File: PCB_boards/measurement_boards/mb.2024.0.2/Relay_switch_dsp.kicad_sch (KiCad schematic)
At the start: 8 parts, among them K1 G5LE-1, K2 G5LE-1, Q1 ZVN4206ASTZ, Q2 ZVN4206ASTZ

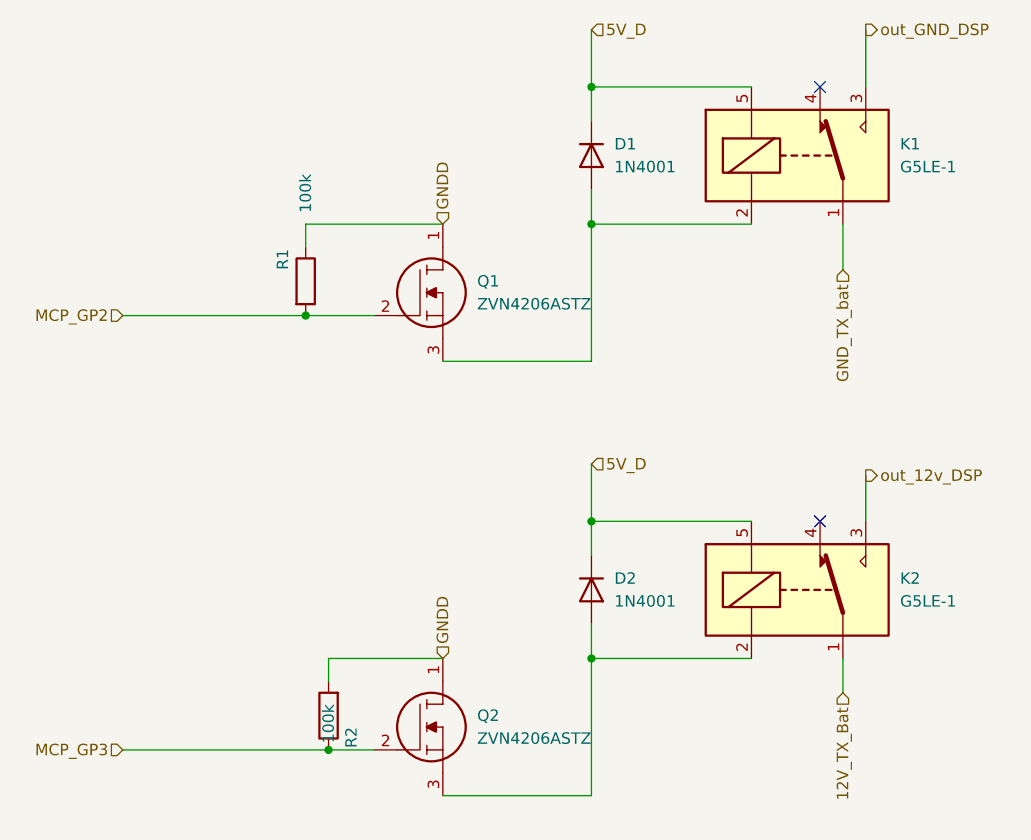
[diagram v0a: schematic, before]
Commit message: correction DPS, add dischage resistor, remove 63 warning on the schemtic, remove 7 errors in schematics change resistor designation, update pcb
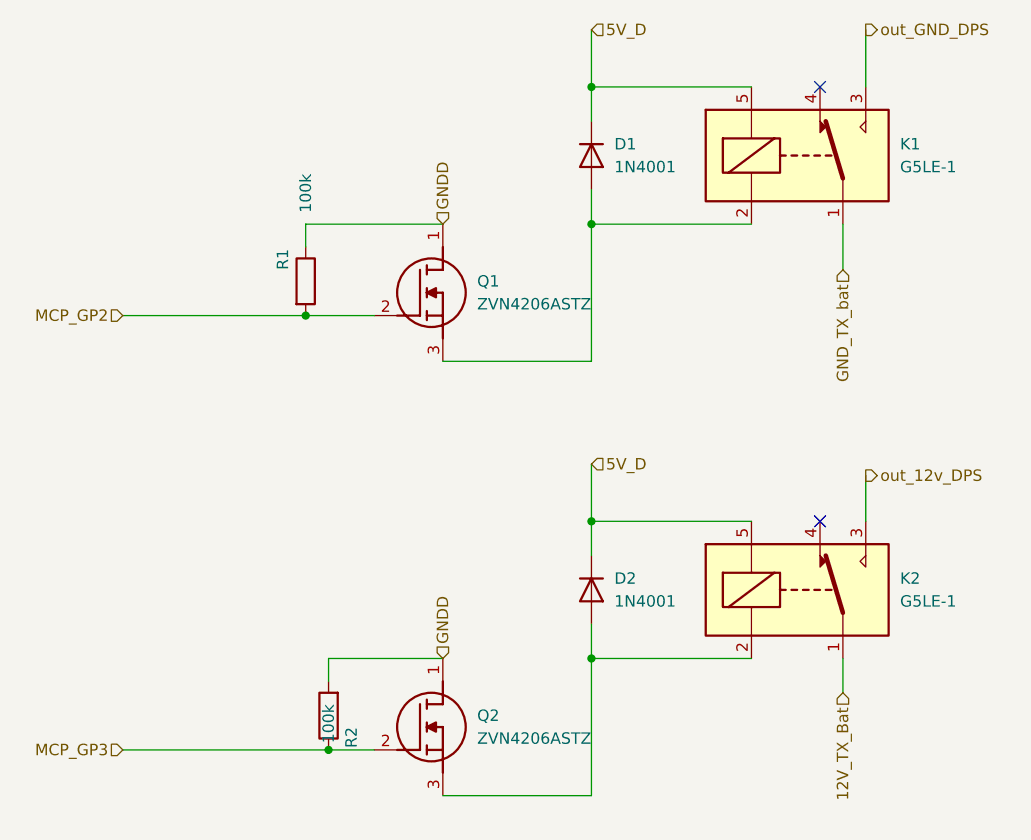
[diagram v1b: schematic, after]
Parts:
- Q1, Q2: symbol ZVN4206A:ZVN4206ASTZ -> ZVN4206ASTZ:ZVN4206ASTZ; Manufacturer_Name Diodes Inc. -> Diodes Incorporated
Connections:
- net out_12v_DSP renamed out_12v_DPS
- net out_GND_DSP renamed out_GND_DPS
